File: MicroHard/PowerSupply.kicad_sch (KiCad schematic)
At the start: 37 parts, among them U1 TPS54325, U2 TPS54294

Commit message: Finish display
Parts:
- added D?: LED, LED_SMD:LED_1206_3216Metric_Pad1.42x1.75mm_HandSolder, symbol Device:LED
- added J?: USB_B_Micro, symbol Connector:USB_B_Micro
- added R?: 68, Resistor_SMD:R_1206_3216Metric_Pad1.30x1.75mm_HandSolder, symbol Device:R
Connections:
- net +3.3V: now also R?.1
- net GND: now also D?.1 (K), J?.5 (GND), J?.6 (Shield)
- net POWER_IN: now also J?.1 (VBUS)
- new net: D?.2 (A), R?.2
- no-connect marks 1 -> 4

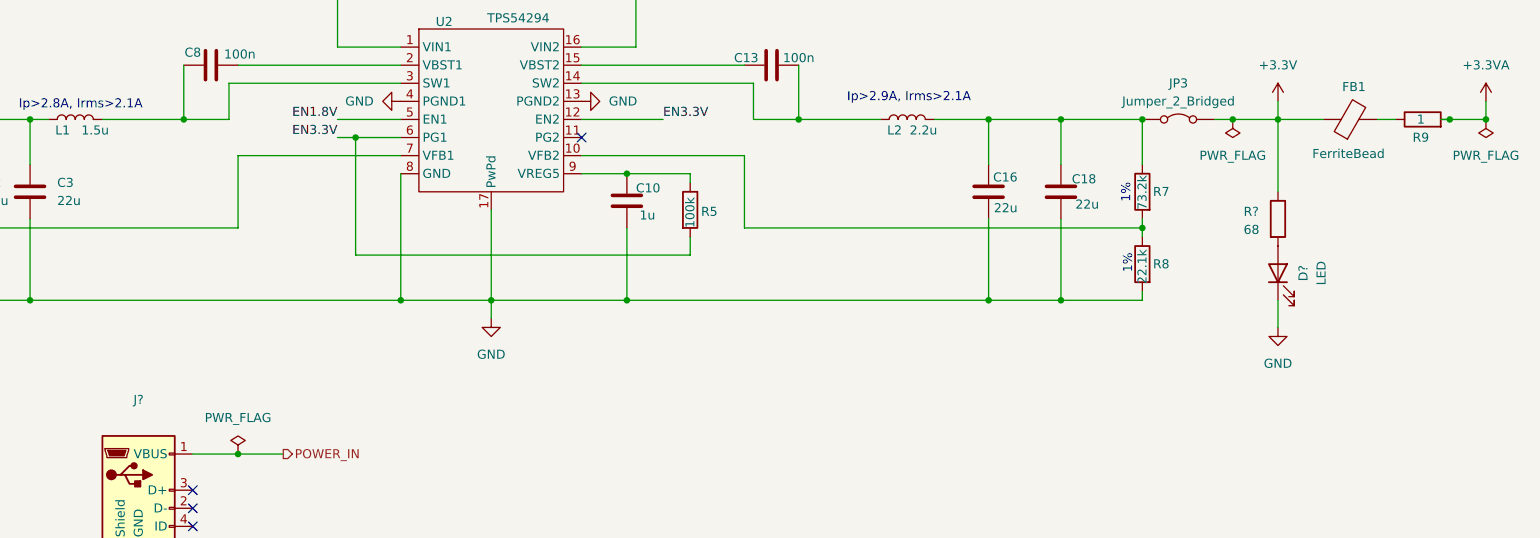
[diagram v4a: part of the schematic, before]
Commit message: Renumber parts
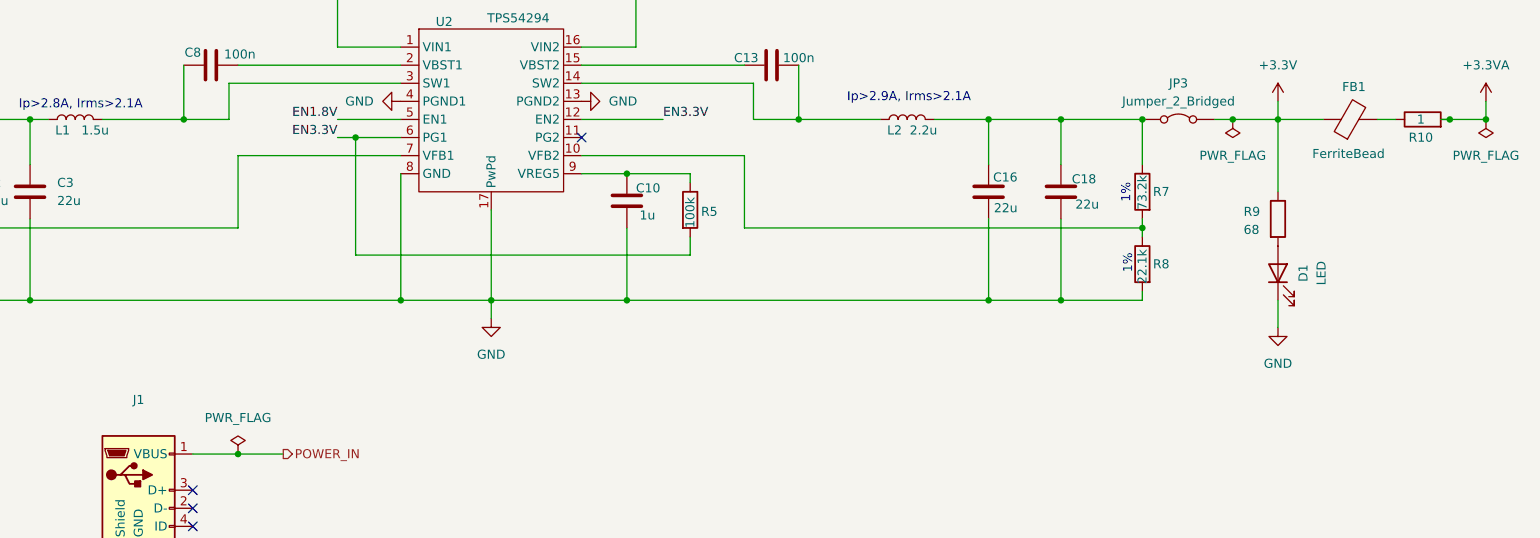
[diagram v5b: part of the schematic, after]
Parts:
- gave numbers to parts that had none: 3
- renumbered R9 to R10
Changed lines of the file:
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@@
 		(dnp no)
 		(fields_autoplaced yes)
-		(property "Reference" "#PWR07"
+		(property "Reference" "#PWR08"
 			(at 245.11 119.38 0)
 			(effects
@@
 			(project ""
 				(path "/578bd531-a491-4b15-a479-460d159ffc14/f6ee64bd-5b5d-4329-b744-4c552611a962"
-					(reference "#PWR07")
+					(reference "#PWR08")
 					(unit 1)
 				)
@@
 		(on_board yes)
 		(dnp no)
-		(property "Reference" "R9"
+		(property "Reference" "R10"
 			(at 265.176 120.65 90)
 			(effects
@@
 			(project ""
 				(path "/578bd531-a491-4b15-a479-460d159ffc14/f6ee64bd-5b5d-4329-b744-4c552611a962"
-					(reference "R9")
+					(reference "R10")
 					(unit 1)
 				)
@@
 		(dnp no)
 		(fields_autoplaced yes)
-		(property "Reference" "#FLG01"
+		(property "Reference" "#FLG02"
 			(at 99.06 163.195 0)
 			(effects
@@
 			(project "MicroHard"
 				(path "/578bd531-a491-4b15-a479-460d159ffc14/f6ee64bd-5b5d-4329-b744-4c552611a962"
-					(reference "#FLG01")
+					(reference "#FLG02")
 					(unit 1)
 				)
@@
 		(dnp no)
 		(fields_autoplaced yes)
-		(property "Reference" "#PWR02"
+		(property "Reference" "#PWR03"
 			(at 115.57 115.57 0)
 			(effects
@@
 			(project "MicroHard"
 				(path "/578bd531-a491-4b15-a479-460d159ffc14/f6ee64bd-5b5d-4329-b744-4c552611a962"
-					(reference "#PWR02")
+					(reference "#PWR03")
 					(unit 1)
 				)
@@
 		(dnp no)
 		(fields_autoplaced yes)
-		(property "Reference" "#PWR08"
+		(property "Reference" "#PWR010"
 			(at 274.32 119.38 0)
 			(effects
@@
 			(project ""
 				(path "/578bd531-a491-4b15-a479-460d159ffc14/f6ee64bd-5b5d-4329-b744-4c552611a962"
-					(reference "#PWR08")
+					(reference "#PWR010")
 					(unit 1)
 				)
@@
 		(dnp no)
 		(fields_autoplaced yes)
-		(property "Reference" "#PWR04"
+		(property "Reference" "#PWR05"
 			(at 134.62 152.4 0)
 			(effects
@@
 			(project "MicroHard"
 				(path "/578bd531-a491-4b15-a479-460d159ffc14/f6ee64bd-5b5d-4329-b744-4c552611a962"
-					(reference "#PWR04")
+					(reference "#PWR05")
 					(unit 1)
 				)
@@
 		(on_board yes)
 		(dnp no)
-		(property "Reference" "D?"
+		(property "Reference" "D1"
 			(at 248.666 139.7 0)
 			(effects
@@
 			(project "MicroHard"
 				(path "/578bd531-a491-4b15-a479-460d159ffc14/f6ee64bd-5b5d-4329-b744-4c552611a962"
-					(reference "D?")
+					(reference "D1")
 					(unit 1)
 				)
@@
 		(on_board yes)
 		(dnp no)
-		(property "Reference" "R?"
+		(property "Reference" "R9"
 			(at 240.284 131.064 0)
 			(effects
@@
 			(project "MicroHard"
 				(path "/578bd531-a491-4b15-a479-460d159ffc14/f6ee64bd-5b5d-4329-b744-4c552611a962"
-					(reference "R?")
+					(reference "R9")
 					(unit 1)
 				)
@@
 		(dnp no)
 		(fields_autoplaced yes)
-		(property "Reference" "#FLG02"
+		(property "Reference" "#FLG01"
 			(at 32.385 114.3 0)
 			(effects
@@
 			(project ""
 				(path "/578bd531-a491-4b15-a479-460d159ffc14/f6ee64bd-5b5d-4329-b744-4c552611a962"
-					(reference "#FLG02")
+					(reference "#FLG01")
 					(unit 1)
 				)
@@
 		(dnp no)
 		(fields_autoplaced yes)
-		(property "Reference" "#PWR03"
+		(property "Reference" "#PWR04"
 			(at 134.62 80.01 0)
 			(effects
@@
 			(project ""
 				(path "/578bd531-a491-4b15-a479-460d159ffc14/f6ee64bd-5b5d-4329-b744-4c552611a962"
-					(reference "#PWR03")
+					(reference "#PWR04")
 					(unit 1)
 				)
@@
 		(dnp no)
 		(fields_autoplaced yes)
-		(property "Reference" "#PWR061"
+		(property "Reference" "#PWR02"
 			(at 85.09 190.5 0)
 			(effects
@@
 			(project "MicroHard"
 				(path "/578bd531-a491-4b15-a479-460d159ffc14/f6ee64bd-5b5d-4329-b744-4c552611a962"
-					(reference "#PWR061")
+					(reference "#PWR02")
 					(unit 1)
 				)
@@
 		(dnp no)
 		(fields_autoplaced yes)
-		(property "Reference" "#PWR062"
+		(property "Reference" "#PWR09"
 			(at 245.11 153.67 0)
 			(effects
@@
 			(project ""
 				(path "/578bd531-a491-4b15-a479-460d159ffc14/f6ee64bd-5b5d-4329-b744-4c552611a962"
-					(reference "#PWR062")
+					(reference "#PWR09")
 					(unit 1)
 				)
@@
 		(dnp no)
 		(fields_autoplaced yes)
-		(property "Reference" "#PWR06"
+		(property "Reference" "#PWR07"
 			(at 245.11 36.83 0)
 			(effects
@@
 			(project ""
 				(path "/578bd531-a491-4b15-a479-460d159ffc14/f6ee64bd-5b5d-4329-b744-4c552611a962"
-					(reference "#PWR06")
+					(reference "#PWR07")
 					(unit 1)
 				)
@@
 		(dnp no)
 		(fields_autoplaced yes)
-		(property "Reference" "J?"
+		(property "Reference" "J1"
 			(at 85.09 157.48 0)
 			(effects
@@
 			(project "MicroHard"
 				(path "/578bd531-a491-4b15-a479-460d159ffc14/f6ee64bd-5b5d-4329-b744-4c552611a962"
-					(reference "J?")
+					(reference "J1")
 					(unit 1)
 				)
@@
 		(dnp no)
 		(fields_autoplaced yes)
-		(property "Reference" "#PWR05"
+		(property "Reference" "#PWR06"
 			(at 153.67 115.57 0)
 			(effects
@@
 			(project "MicroHard"
 				(path "/578bd531-a491-4b15-a479-460d159ffc14/f6ee64bd-5b5d-4329-b744-4c552611a962"
-					(reference "#PWR05")
+					(reference "#PWR06")
 					(unit 1)
 				)

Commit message: footprints
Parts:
- C1: footprint (none) -> Capacitor_SMD:C_1210_3225Metric_Pad1.33x2.70mm_HandSolder
- C10, C11, C12, C13, C14, C15, C16, C17, C18, C19, C2, C3, C4, C5, C6, C7, C8, C9: footprint (none) -> Capacitor_SMD:C_1206_3216Metric_Pad1.33x1.80mm_HandSolder
- FB1, R1, R10, R2, R3, R4, R5, R6, R7, R8: footprint (none) -> Resistor_SMD:R_1206_3216Metric_Pad1.30x1.75mm_HandSolder
- JP1, JP2, JP3: footprint (none) -> Connector_PinHeader_2.54mm:PinHeader_1x02_P2.54mm_Vertical
- L1, L2, L3: footprint (none) -> Inductor_SMD:L_1206_3216Metric_Pad1.42x1.75mm_HandSolder
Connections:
- no-connect marks 4 -> 5

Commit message: Small fixes
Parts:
- J1: footprint (none) -> Connector_USB:USB_Micro-B_Amphenol_10118194_Horizontal
- U1: footprint (none) -> TPS54325PWP:PWP14_2P31X2P46
- U2: footprint (none) -> TPS54294PWP:PWP16_2P31X2P46
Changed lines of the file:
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@@
 	)
 	(junction
-		(at 99.06 165.1)
-		(diameter 0)
-		(color 0 0 0 0)
-	)
-	(junction
 		(at 121.92 71.12)
 		(diameter 0)
@@
 	)
 	(junction
-		(at 134.62 73.66)
-		(diameter 0)
-		(color 0 0 0 0)
-	)
-	(junction
 		(at 116.84 41.91)
 		(diameter 0)
@@
 	(wire
 		(pts
-			(xy 99.06 165.1) (xy 105.41 165.1)
+			(xy 245.11 118.11) (xy 245.11 115.57)
 		)
 		(stroke
@@
 	(wire
 		(pts
-			(xy 245.11 118.11) (xy 245.11 115.57)
+			(xy 81.28 96.52) (xy 81.28 100.33)
 		)
 		(stroke
@@
 	(wire
 		(pts
-			(xy 81.28 96.52) (xy 81.28 100.33)
+			(xy 162.56 137.16) (xy 162.56 134.62)
 		)
 		(stroke
@@
 	(wire
 		(pts
-			(xy 162.56 137.16) (xy 162.56 134.62)
+			(xy 267.97 118.11) (xy 269.24 118.11)
 		)
 		(stroke
@@
 	(wire
 		(pts
-			(xy 267.97 118.11) (xy 269.24 118.11)
+			(xy 59.69 143.51) (xy 69.85 143.51)
 		)
 		(stroke
@@
 	(wire
 		(pts
-			(xy 59.69 143.51) (xy 69.85 143.51)
+			(xy 204.47 132.08) (xy 204.47 143.51)
 		)
 		(stroke
@@
 	(wire
 		(pts
-			(xy 204.47 132.08) (xy 204.47 143.51)
+			(xy 116.84 52.07) (xy 121.92 52.07)
 		)
 		(stroke
@@
 	(wire
 		(pts
-			(xy 116.84 52.07) (xy 121.92 52.07)
+			(xy 92.71 165.1) (xy 104.14 165.1)
 		)
 		(stroke
@@
 	(wire
 		(pts
-			(xy 92.71 165.1) (xy 99.06 165.1)
-		)
-		(stroke
-			(width 0)
-			(type default)
-		)
-	)
-	(wire
-		(pts
 			(xy 59.69 39.37) (xy 59.69 41.91)
 		)
@@
 		)
 	)
-	(label "EN1.8V"
-		(at 113.03 118.11 180)
+	(label "POWER_IN"
+		(at 46.99 39.37 0)
 		(fields_autoplaced yes)
 		(effects
@@
 				(size 1.27 1.27)
 			)
-			(justify right bottom)
+			(justify left bottom)
 		)
 	)
-	(label "EN3.3V"
-		(at 113.03 120.65 180)
+	(label "EN1.8V"
+		(at 113.03 118.11 180)
 		(fields_autoplaced yes)
 		(effects
@@
 	)
 	(label "EN3.3V"
-		(at 158.75 118.11 0)
+		(at 113.03 120.65 180)
 		(fields_autoplaced yes)
 		(effects
@@
 				(size 1.27 1.27)
 			)
-			(justify left bottom)
+			(justify right bottom)
 		)
 	)
-	(label "EN1.8V"
-		(at 182.88 57.15 0)
+	(label "POWER_IN"
+		(at 104.14 165.1 0)
 		(fields_autoplaced yes)
 		(effects
@@
 		)
 	)
-	(hierarchical_label "POWER_IN"
-		(shape output)
-		(at 105.41 165.1 0)
+	(label "POWER_IN"
+		(at 46.99 100.33 0)
+		(fields_autoplaced yes)
 		(effects
 			(font
 				(size 1.27 1.27)
 			)
-			(justify left)
-		)
-		(property "untitled" "4.5V - 18V"
-			(at 108.458 167.894 0)
-			(effects
-				(font
-					(size 1.27 1.27)
-					(italic yes)
-				)
-				(justify right)
-			)
+			(justify left bottom)
 		)
 	)
-	(hierarchical_label "POWER_IN"
-		(shape input)
-		(at 46.99 39.37 180)
+	(label "EN3.3V"
+		(at 158.75 118.11 0)
+		(fields_autoplaced yes)
 		(effects
 			(font
 				(size 1.27 1.27)
 			)
-			(justify right)
-		)
-		(property "untitled" "4.5V - 18V"
-			(at 50.038 42.164 0)
-			(effects
-				(font
-					(size 1.27 1.27)
-					(italic yes)
-				)
-				(justify right)
-			)
+			(justify left bottom)
 		)
 	)
-	(hierarchical_label "POWER_IN"
-		(shape input)
-		(at 46.99 100.33 180)
+	(label "EN1.8V"
+		(at 182.88 57.15 0)
+		(fields_autoplaced yes)
 		(effects
 			(font
 				(size 1.27 1.27)
 			)
-			(justify right)
-		)
-		(property "untitled" "4.5V - 18V"
-			(at 50.038 103.124 0)
-			(effects
-				(font
-					(size 1.27 1.27)
-					(italic yes)
-				)
-				(justify right)
-			)
+			(justify left bottom)
 		)
 	)
@@
 	)
 	(symbol
-		(lib_id "power:PWR_FLAG")
-		(at 99.06 165.1 0)
-		(unit 1)
-		(exclude_from_sim no)
-		(in_bom yes)
-		(on_board yes)
-		(dnp no)
-		(fields_autoplaced yes)
-		(property "Reference" "#FLG02"
-			(at 99.06 163.195 0)
-			(effects
-				(font
-					(size 1.27 1.27)
-				)
-				(hide yes)
-			)
-		)
-		(property "Value" "PWR_FLAG"
-			(at 99.06 160.02 0)
-			(effects
-				(font
-					(size 1.27 1.27)
-				)
-			)
-		)
-		(property "Footprint" ""
-			(at 99.06 165.1 0)
-			(effects
-				(font
-					(size 1.27 1.27)
-				)
-				(hide yes)
-			)
-		)
-		(property "Datasheet" "~"
-			(at 99.06 165.1 0)
-			(effects
-				(font
-					(size 1.27 1.27)
-				)
-				(hide yes)
-			)
-		)
-		(property "Description" "Special symbol for telling ERC where power comes from"
-			(at 99.06 165.1 0)
-			(effects
-				(font
-					(size 1.27 1.27)
-				)
-				(hide yes)
-			)
-		)
-		(pin "1"
-		)
-		(instances
-			(project "MicroHard"
-				(path "/578bd531-a491-4b15-a479-460d159ffc14/f6ee64bd-5b5d-4329-b744-4c552611a962"
-					(reference "#FLG02")
-					(unit 1)
-				)
-			)
-		)
-	)
-	(symbol
 		(lib_id "Device:FerriteBead")
 		(at 255.27 118.11 90)
@@
 	)
 	(symbol
-		(lib_id "power:PWR_FLAG")
-		(at 134.62 73.66 90)
-		(unit 1)
-		(exclude_from_sim no)
-		(in_bom yes)
-		(on_board yes)
-		(dnp no)
-		(fields_autoplaced yes)
-		(property "Reference" "#FLG03"
-			(at 132.715 73.66 0)
-			(effects
-				(font
-					(size 1.27 1.27)
-				)
-				(hide yes)
-			)
-		)
-		(property "Value" "PWR_FLAG"
-			(at 130.81 73.6599 90)
-			(effects
-				(font
-					(size 1.27 1.27)
-				)
-				(justify left)
-			)
-		)
-		(property "Footprint" ""
-			(at 134.62 73.66 0)
-			(effects
-				(font
-					(size 1.27 1.27)
-				)
-				(hide yes)
-			)
-		)
-		(property "Datasheet" "~"
-			(at 134.62 73.66 0)
-			(effects
-				(font
-					(size 1.27 1.27)
-				)
-				(hide yes)
-			)
-		)
-		(property "Description" "Special symbol for telling ERC where power comes from"
-			(at 134.62 73.66 0)
-			(effects
-				(font
-					(size 1.27 1.27)
-				)
-				(hide yes)
-			)
-		)
-		(pin "1"
-		)
-		(instances
-			(project ""
-				(path "/578bd531-a491-4b15-a479-460d159ffc14/f6ee64bd-5b5d-4329-b744-4c552611a962"
-					(reference "#FLG03")
-					(unit 1)
-				)
-			)
-		)
-	)
-	(symbol
 		(lib_id "power:GND")
 		(at 134.62 146.05 0)
@@
 			)
 		)
-		(property "Footprint" ""
+		(property "Footprint" "TPS54294PWP:PWP16_2P31X2P46"
 			(at 118.11 113.03 0)
 			(effects
@@
 			)
 		)
-		(property "Footprint" ""
+		(property "Footprint" "Connector_USB:USB_Micro-B_Amphenol_10118194_Horizontal"
 			(at 88.9 171.45 0)
 			(effects
@@
 			)
 		)
-		(property "Footprint" ""
+		(property "Footprint" "TPS54325PWP:PWP14_2P31X2P46"
 			(at 128.27 44.45 0)
 			(effects

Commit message: Initial layout
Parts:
- renumbered C15 to C1, C7 to C10, C12 to C11, C14 to C12, C8 to C13, C13 to C14, C2 to C15, C3 to C16, C16 to C17, C10 to C19, C1 to C2, C4 to C3, C6 to C4, C17 to C5, C19 to C6, C9 to C7, C11 to C8, C5 to C9, JP2 to JP1, JP1 to JP2, L3 to L1, L1 to L2, L2 to L3, R3 to R1, R8 to R10, R6 to R2, R4 to R3, R10 to R4, R1 to R5, R7 to R6, R5 to R7, R9 to R8, R2 to R9
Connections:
- net +1V8: now also JP2.2 (B); no longer JP2.1 (A)
- net at C15.1, C16.1, L2.1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: now also JP2.1 (A); no longer JP2.2 (B)
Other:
- moved on the sheet: JP2
